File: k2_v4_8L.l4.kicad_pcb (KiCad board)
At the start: 8 copper layers, 120 x 46 mm, 42 parts, among them J11 J_EC_HEADER, J12 J_12V_IN, J13 J_SWD, J2 SlimSAS_x8_SFF8654, J3 MCIO_4i_SFF1016, J4 MCIO_4i_SFF1016, J6 J_PWR_CTRL, J9 J_OOB_HEADER, U1 STM32G0B1CBT6, U2 DCDC_12V_3V3, U4 BAT54C, U5 OPTO_LTV356T, U6 DS320PR1601

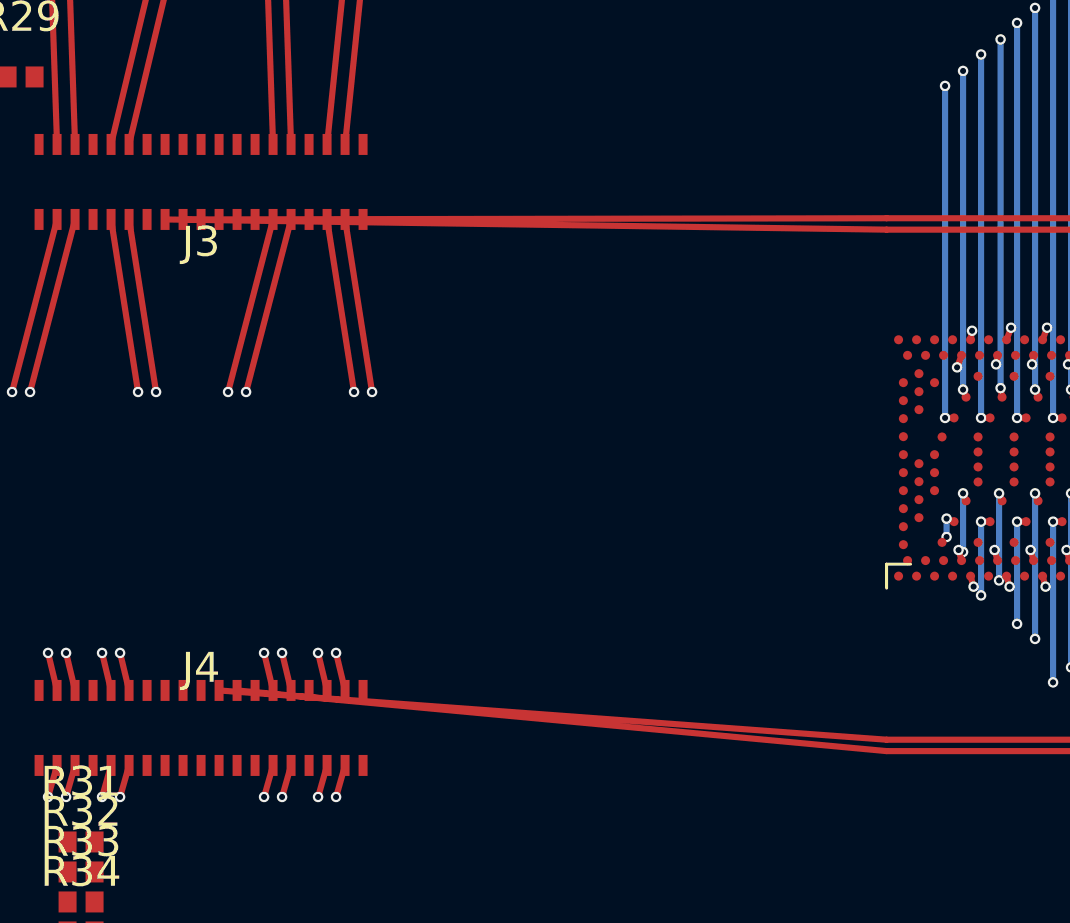
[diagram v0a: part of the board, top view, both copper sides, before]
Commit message: CO-43: 远端 J3/J4 REFCLK 接入落地（两排间自由带 + 抬升列 65.55/66.05 + 2 选 1 交叉自检 + 垂直接入 pad）— 引擎 FEASIBLE_ALL/work 546/546、L4 PASS（segs 2419/vias 252）、DFM new 54->38（mask 36->18）；已记两处实现缺陷修正（远近标签写反、抬升列误落 A 排内）
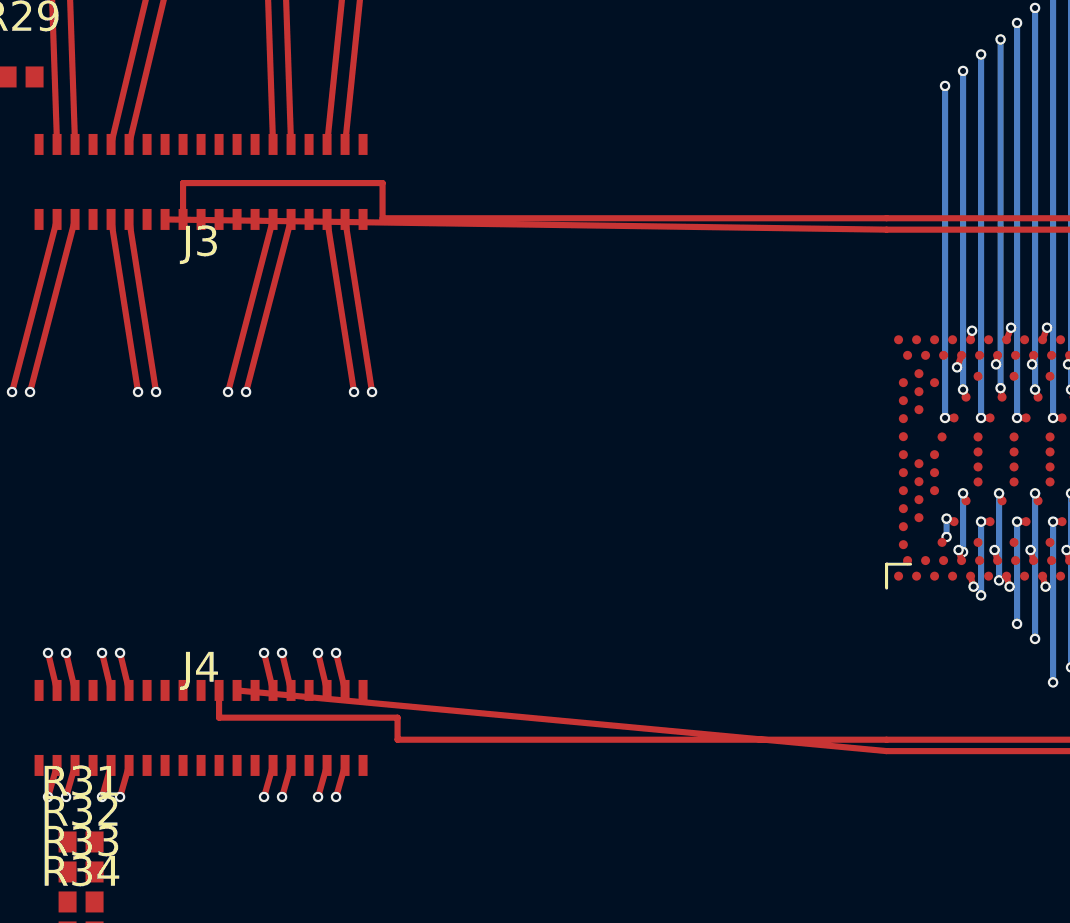
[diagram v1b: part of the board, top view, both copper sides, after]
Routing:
- net PCIE_REFCLK0_P: track 73.9 -> 76.3 mm
- net PCIE_REFCLK1_P: track 84.8 -> 86.4 mm

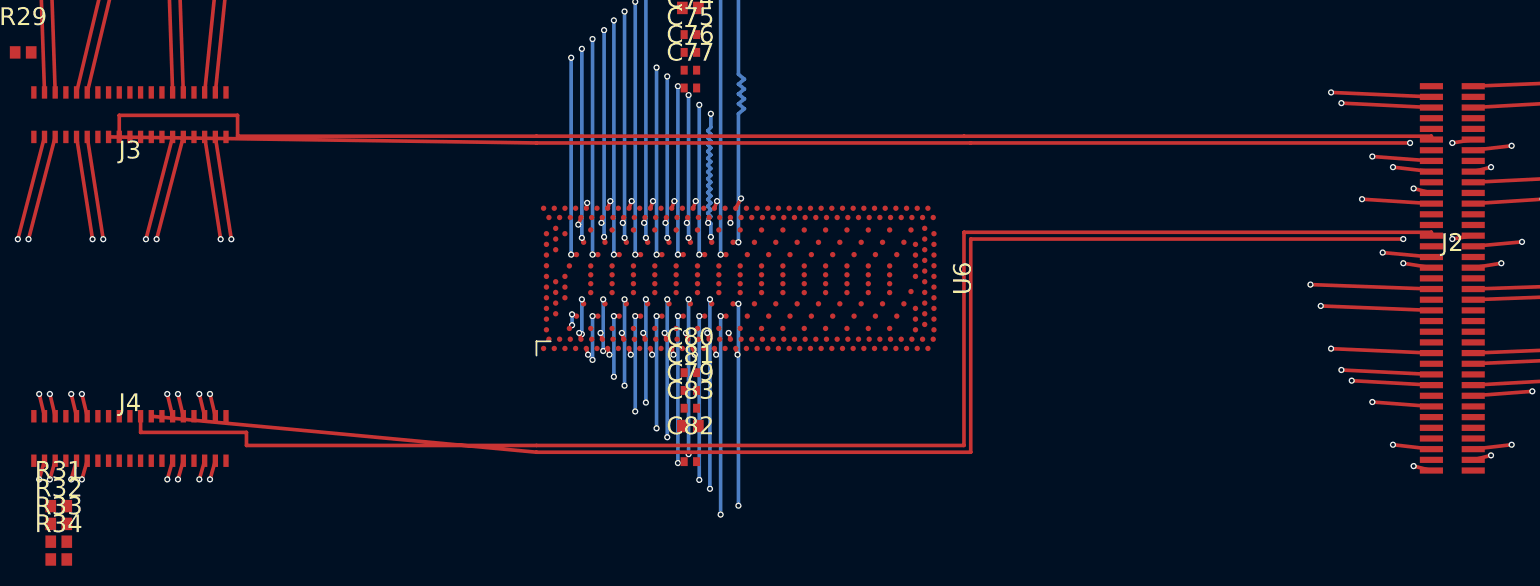
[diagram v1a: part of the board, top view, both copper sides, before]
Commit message: CO-45: REFCLK 收敛收官 — G7/L5 DFM new 38→0（G4..G7 全 PASS）
L2 自裁实施（无 L1 变更），引擎 rev W3-CN.40：
- 对内偏移 REFCLK_OFF {P:0.0, N:-0.5}：P 由 pad 中心线直出 ⇒ J2 P jog=0（消 0.1325×2）；
  N 北移 0.5（边距 0.295）⇒ 消对内 0.1734 与 N via#2 vs P 轨 0.1025（ECS_DX 0.4525）。
- ECS-001 dip 解耦：via1_y（pad 直出 stub，受 pad10/14 净距）与 dip_y（N 轨 y）解耦，绕行闭式。
- 远端接入闭式化（取代 CO-43 的 2 选 1 启发）：N 北线/P 南线 + P 西列/N 东列，FAR_LINE_STEP 0.38→0.5，
  函数内真实线段相交自检（相交即停机）；远端 waypoint 统一补入 3D nodes（修 CO-43 图纸/nodes 不一致）。
- P 轨等长幂绕（闭式 n,h,A，幅值 ≤2.0）保证残余 skew ≤0.15（SPEC 不放宽）。
- 新增 A-CN.5d（引擎 + 独立验证器 v2 复算）：REFCLK 同层 P/N（含页间）交叉 = 0（教训 1）。
- L5 SI 纳入 REFCLK 页（net_class PCIe85 ⇒ 原跳过非 data 页为漏判），现覆盖 34 页。

本续接会话修复的 G-M3 探针缺陷（方法门保真度，非判据放宽；真实板路径逐字节不变）：
- --scale 副本仅平移 pad 锚点而 REFCLK 构造消费绝对板框常量 ⇒ 幂绕带 span 变负误报不可行；
- 探针剔除 data 页 ⇒ _far_row_span 只取单排 ⇒ 远端折叠成直线 stub（未构造远端接入）。
  修复后 G-M3：K=2 work=1076 / K=4 work=2152 / per_copy=538，线性成立。

门禁：G4 FEASIBLE_ALL W3-CN.40 dfa1d7c4a811b0da（A-CN.1..9 + A-CN.5d=0、crossings 0、work 546/546）；
G5 validator v2 PASS（G-M1..6、A1.2/A1.3/A1.4、frozen=True）；G6 L4 PASS（板 4d36212f6492262b、
68 网/2441 段/252 via、viol 0）；G7 FAB ok / SI PASS（skew 0.0031 ≤ 0.15，34 页）/ DFM PASS new=0
（铜层违规 0；余 42 条 = 冻结基线 lib/silk，计入不计）。

CO-44 的「witness v2 输入缺口」判读修正：对内 0.5 由北移 N 达成（A-CN.5a=0 未触 C80 盒）、远端 mask 随
带内线北移出开窗并经 A-CN.5d/DRC 复核归零 ⇒ CO-25 v1 witness v2 不再阻塞 D3a（存档保留）。

红线：四冻结源 4/4 MATCH 未动；.kicad_dru 3148703240d54420 未改（逃逸区显式排除 REFCLK ⇒ 未掩盖）；
intra_pair_skew/净距阈值未放宽；while=0、零坐标搜索。
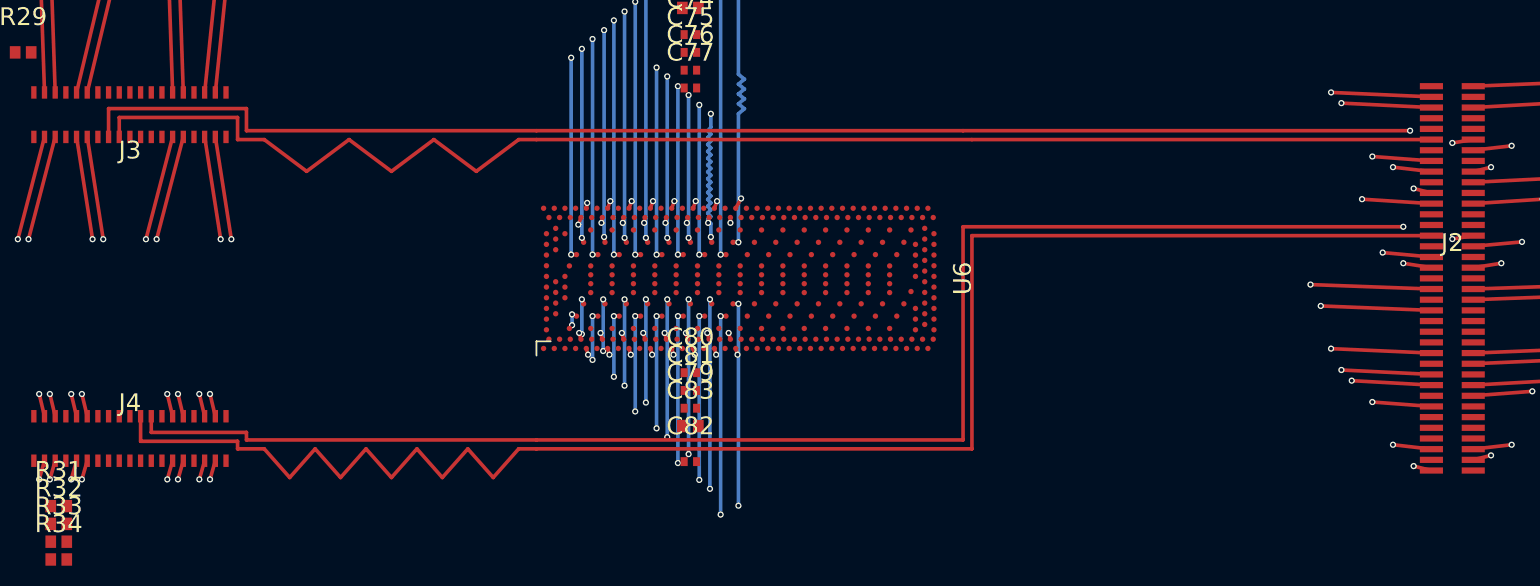
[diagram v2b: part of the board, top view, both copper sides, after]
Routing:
- net PCIE_REFCLK1_P: track 86.4 -> 93.6 mm
- net PCIE_REFCLK0_P: track 76.3 -> 79.6 mm
- net PCIE_REFCLK0_N: track 76.7 -> 79.6 mm
- net PCIE_REFCLK1_N: track 93.1 -> 93.6 mm
